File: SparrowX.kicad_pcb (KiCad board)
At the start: 4 copper layers, 31.6 x 26.6 mm, 25 parts, among them J1 NORTH, J2 SOUTH, J3 WEST, J4 EAST, U1 TPS629210-Q1, U2 LD49100PU33RY, U3 STM32G0B1CBU6, U4 TCAN332G, U5 TCAN332G

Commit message: Everybody gets more vias!
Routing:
- net /PA0: track 7.64 -> 10.5 mm
- net VDC: track 37.8 -> 39.1 mm
- net /~{RESET}: track 31.0 -> 29.8 mm
- net /CAN0_TX: track 8.87 -> 9.97 mm
- net /PA10: track 18.7 -> 19.2 mm
- net /PB14: track 20.9 -> 21.4 mm
- net GND: vias 29 -> 85
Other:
- board text added: "2"

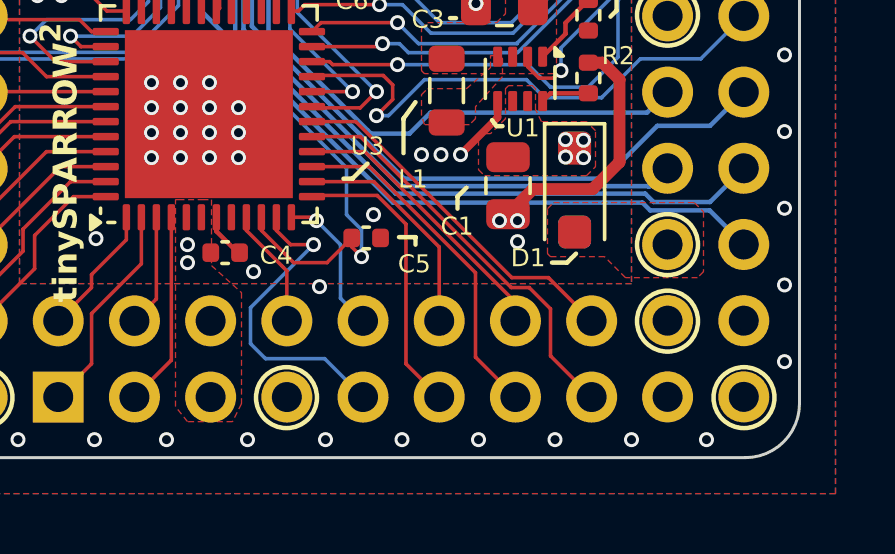
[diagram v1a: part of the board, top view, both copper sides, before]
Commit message: Oops: fix missing PF0 pin
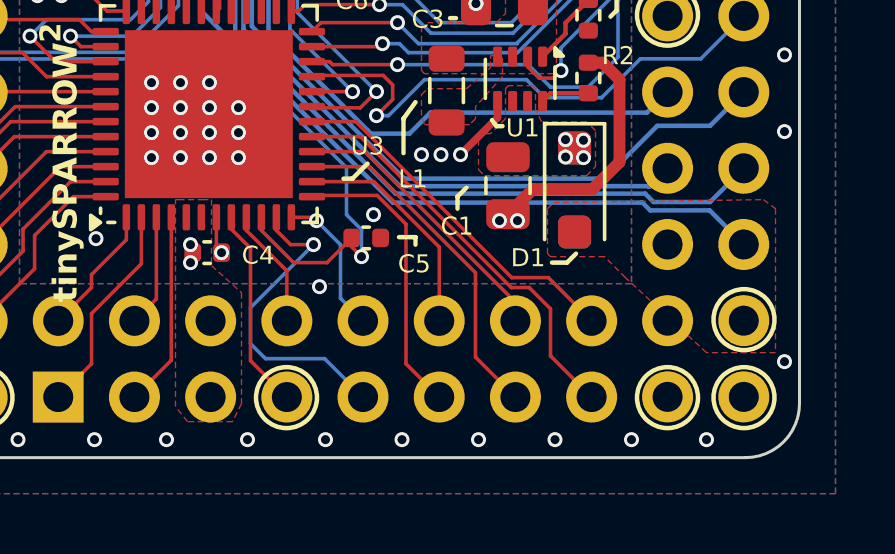
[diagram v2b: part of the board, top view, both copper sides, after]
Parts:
- moved C4 0.60 mm to (166.5, 100.6)
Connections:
- J2 pad 7: GND -> /PF0
- J4 pad 15: VDC -> unconnected-(J4-Pin_15-Pad15)
- J4 pad 17: GND -> unconnected-(J4-Pin_17-Pad17)
- J4 pad 18: unconnected-(J4-Pin_18-Pad18) -> VDC
- J4 pad 19: unconnected-(J4-Pin_19-Pad19) -> GND
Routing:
- net /PF0: track 0.00 -> 6.76 mm
- net VDC: track 39.1 -> 42.0 mm
- net GND: track 12.3 -> 12.0 mm, vias 85 -> 82
- added copper zone on In2.Cu, net VDC
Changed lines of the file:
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@@
 	(net 70 "unconnected-(U5-NC-Pad5)")
 	(net 71 "unconnected-(U5-NC-Pad8)")
-	(net 72 "unconnected-(J4-Pin_19-Pad19)")
-	(net 73 "unconnected-(J4-Pin_18-Pad18)")
+	(net 72 "unconnected-(J4-Pin_17-Pad17)")
+	(net 73 "unconnected-(J4-Pin_15-Pad15)")
 	(net 74 "unconnected-(U2-PG-Pad3)")
 	(footprint "Capacitor_SMD:C_0402_1005Metric"
@@
 	(footprint "Capacitor_SMD:C_0402_1005Metric"
 		(layer "F.Cu")
-		(at 167.0548 100.5672)
+		(at 166.4548 100.5672)
 		(descr "Capacitor SMD 0402 (1005 Metric), square (rectangular) end terminal, IPC_7351 nominal, (Body size source: IPC-SM-782 page 76, https://www.pcb-3d.com/wordpress/wp-content/uploads/ipc-sm-782a_amendment_1_and_2.pdf), generated with kicad-footprint-generator")
 		(tags "capacitor")
@@
 			(layers "*.Cu" "*.Mask")
 			(remove_unused_layers no)
-			(net 1 "GND")
+			(net 52 "/PF0")
 			(pinfunction "Pin_7")
 			(pintype "passive")
@@
 			(layers "*.Cu" "*.Mask")
 			(remove_unused_layers no)
-			(net 10 "VDC")
+			(net 73 "unconnected-(J4-Pin_15-Pad15)")
 			(pinfunction "Pin_15")
-			(pintype "passive")
+			(pintype "passive+no_connect")
 		)
 		(pad "16" thru_hole oval
@@
 			(layers "*.Cu" "*.Mask")
 			(remove_unused_layers no)
-			(net 1 "GND")
+			(net 72 "unconnected-(J4-Pin_17-Pad17)")
 			(pinfunction "Pin_17")
-			(pintype "passive")
+			(pintype "passive+no_connect")
 		)
 		(pad "18" thru_hole oval
@@
 			(layers "*.Cu" "*.Mask")
 			(remove_unused_layers no)
-			(net 73 "unconnected-(J4-Pin_18-Pad18)")
+			(net 10 "VDC")
 			(pinfunction "Pin_18")
-			(pintype "passive+no_connect")
+			(pintype "passive")
 		)
 		(pad "19" thru_hole oval
@@
 			(layers "*.Cu" "*.Mask")
 			(remove_unused_layers no)
-			(net 72 "unconnected-(J4-Pin_19-Pad19)")
+			(net 1 "GND")
 			(pinfunction "Pin_19")
-			(pintype "passive+no_connect")
+			(pintype "passive")
 		)
 		(pad "20" thru_hole oval
@@
 	)
 	(gr_circle
-		(center 181.8 102.85)
-		(end 181.8 101.834)
+		(center 181.8 105.4)
+		(end 181.8 104.384)
 		(stroke
 			(width 0.15)
@@
 	)
 	(gr_circle
-		(center 181.8 100.3)
-		(end 182.816 100.3)
+		(center 184.35 102.8)
+		(end 185.366 102.8)
 		(stroke
 			(width 0.15)
@@
 	)
 	(segment
-		(start 166.762136 99.387764)
-		(end 166.762136 99.853756)
-		(width 0.15)
+		(start 176.1378 96.0622)
+		(end 174.9 97.3)
+		(width 0.25)
 		(layer "F.Cu")
 		(net 1)
 	)
 	(segment
-		(start 167.47558 100.5672)
-		(end 167.5348 100.5672)
-		(width 0.15)
+		(start 177.317599 98.45)
+		(end 176.4828 99.284799)
+		(width 0.4)
 		(layer "F.Cu")
 		(net 1)
 	)
 	(segment
-		(start 176.1378 96.0622)
-		(end 174.9 97.3)
-		(width 0.25)
+		(start 166.762136 99.387764)
+		(end 166.762136 100.394536)
+		(width 0.12)
 		(layer "F.Cu")
 		(net 1)
 	)
 	(segment
-		(start 177.317599 98.45)
-		(end 176.4828 99.284799)
-		(width 0.4)
+		(start 166.762136 100.394536)
+		(end 166.9348 100.5672)
+		(width 0.12)
 		(layer "F.Cu")
 		(net 1)
@@
 		(net 1)
 	)
-	(segment
-		(start 166.762136 99.853756)
-		(end 167.47558 100.5672)
-		(width 0.15)
-		(layer "F.Cu")
-		(net 1)
-	)
 	(via
 		(at 161.6 92)
@@
 	)
 	(via
-		(at 168 101.2)
-		(size 0.5)
-		(drill 0.3)
-		(layers "F.Cu" "B.Cu")
-		(free yes)
-		(net 1)
-	)
-	(via
 		(at 166.533332 95.733333)
 		(size 0.5)
@@
 	)
 	(via
-		(at 176.8 100.2)
-		(size 0.5)
-		(drill 0.3)
-		(layers "F.Cu" "B.Cu")
-		(free yes)
-		(net 1)
-	)
-	(via
 		(at 165.1 106.8)
 		(size 0.5)
@@
 	)
 	(via
-		(at 185.7 101.64375)
-		(size 0.5)
-		(drill 0.3)
-		(layers "F.Cu" "B.Cu")
-		(free yes)
-		(net 1)
-	)
-	(via
 		(at 162.75 100.1)
 		(size 0.5)
@@
 	)
 	(via
-		(at 185.7 99.0875)
-		(size 0.5)
-		(drill 0.3)
-		(layers "F.Cu" "B.Cu")
-		(free yes)
-		(net 1)
-	)
-	(via
 		(at 175.415201 92.262801)
 		(size 0.5)
@@
 	)
 	(via
+		(at 166.9348 100.5672)
+		(size 0.5)
+		(drill 0.3)
+		(layers "F.Cu" "B.Cu")
+		(net 1)
+	)
+	(via
 		(at 178.15 81.2)
 		(size 0.5)
@@
 	)
 	(via
-		(at 165.8 100.9)
+		(at 165.9 100.9)
 		(size 0.5)
 		(drill 0.3)
@@
 	)
 	(via
-		(at 165.8 100.3)
+		(at 165.9 100.3)
 		(size 0.5)
 		(drill 0.3)
@@
 	)
 	(segment
-		(start 162.7844 83.8218)
-		(end 162.7844 86.5844)
+		(start 162.7844 86.5844)
+		(end 163.5 87.3)
 		(width 0.4)
 		(layer "In2.Cu")
@@
 	)
 	(segment
-		(start 162.7844 86.5844)
-		(end 163.5 87.3)
+		(start 169.5 98.3)
+		(end 172.8 98.3)
 		(width 0.4)
 		(layer "In2.Cu")
@@
 	)
 	(segment
-		(start 163.5 94.3)
-		(end 162 95.8)
+		(start 175.2 100.7)
+		(end 179.6 100.7)
 		(width 0.4)
 		(layer "In2.Cu")
@@
 	)
 	(segment
-		(start 163 99.1)
-		(end 168.7 99.1)
+		(start 179.6 100.7)
+		(end 180.4448 101.5448)
 		(width 0.4)
 		(layer "In2.Cu")
@@
 	)
 	(segment
-		(start 162 98.1)
-		(end 163 99.1)
+		(start 163.5 94.3)
+		(end 162 95.8)
 		(width 0.4)
 		(layer "In2.Cu")
@@
 	)
 	(segment
-		(start 169.5 98.3)
-		(end 172.8 98.3)
+		(start 172.8 98.3)
+		(end 175.2 100.7)
 		(width 0.4)
 		(layer "In2.Cu")
@@
 	)
 	(segment
-		(start 179.1 101.1)
-		(end 179.9052 100.2948)
+		(start 163 99.1)
+		(end 168.7 99.1)
 		(width 0.4)
 		(layer "In2.Cu")
@@
 	)
 	(segment
-		(start 179.9052 100.2948)
-		(end 181.8024 100.2948)
+		(start 162 95.8)
+		(end 162 98.1)
 		(width 0.4)
 		(layer "In2.Cu")
@@
 	)
 	(segment
-		(start 163.5 87.3)
-		(end 163.5 94.3)
+		(start 180.4448 101.5448)
+		(end 183.0524 101.5448)
 		(width 0.4)
 		(layer "In2.Cu")
@@
 	)
 	(segment
-		(start 175.6 101.1)
-		(end 179.1 101.1)
+		(start 162 98.1)
+		(end 163 99.1)
 		(width 0.4)
 		(layer "In2.Cu")
@@
 	)
 	(segment
-		(start 162 95.8)
-		(end 162 98.1)
+		(start 161.4944 82.5318)
+		(end 162.7844 83.8218)
 		(width 0.4)
 		(layer "In2.Cu")
@@
 	)
 	(segment
-		(start 161.4944 82.5318)
-		(end 162.7844 83.8218)
+		(start 163.5 87.3)
+		(end 163.5 94.3)
 		(width 0.4)
 		(layer "In2.Cu")
@@
 	)
 	(segment
-		(start 172.8 98.3)
-		(end 175.6 101.1)
+		(start 183.0524 101.5448)
+		(end 184.3424 102.8348)
+		(width 0.4)
+		(layer "In2.Cu")
+		(net 10)
+	)
+	(segment
+		(start 162.7844 83.8218)
+		(end 162.7844 86.5844)
 		(width 0.4)
 		(layer "In2.Cu")
@@
 	)
 	(segment
+		(start 167.9 100.420944)
+		(end 167.9 104.1692)
+		(width 0.12)
+		(layer "F.Cu")
+		(net 52)
+	)
+	(segment
+		(start 167.262136 99.78308)
+		(end 167.9 100.420944)
+		(width 0.12)
+		(layer "F.Cu")
+		(net 52)
+	)
+	(segment
+		(start 167.9 104.1692)
+		(end 169.1116 105.3808)
+		(width 0.12)
+		(layer "F.Cu")
+		(net 52)
+	)
+	(segment
+		(start 167.262136 99.387764)
+		(end 167.262136 99.78308)
+		(width 0.12)
+		(layer "F.Cu")
+		(net 52)
+	)
+	(segment
 		(start 169.1116 102.8408)
 		(end 169.1116 101.174728)
@@
 		(net 10)
 		(net_name "VDC")
-		(layer "F.Cu")
+		(layers "F.Cu" "In2.Cu")
 		(name "VDC_IN")
 		(hatch edge 0.5)
 		(priority 7)
 		(connect_pads yes
-			(clearance 0.5)
+			(clearance 0.3)
 		)
-		(min_thickness 0.25)
+		(min_thickness 0.15)
 		(filled_areas_thickness no)
 		(fill yes
@@
 		(polygon
 			(pts
-				(xy 177.8 100.6) (xy 177.8 99.1) (xy 178 98.9) (xy 182.7 98.9) (xy 183 99.2) (xy 183 101.2) (xy 182.8 101.4)
+				(xy 177.8 100.6) (xy 177.8 99.1) (xy 178 98.9) (xy 185 98.8) (xy 185.4 99.1) (xy 185.4 103.9) (xy 183.1 103.9)
 				(xy 180.4 101.4) (xy 179.7 100.7) (xy 177.9 100.7)
 			)

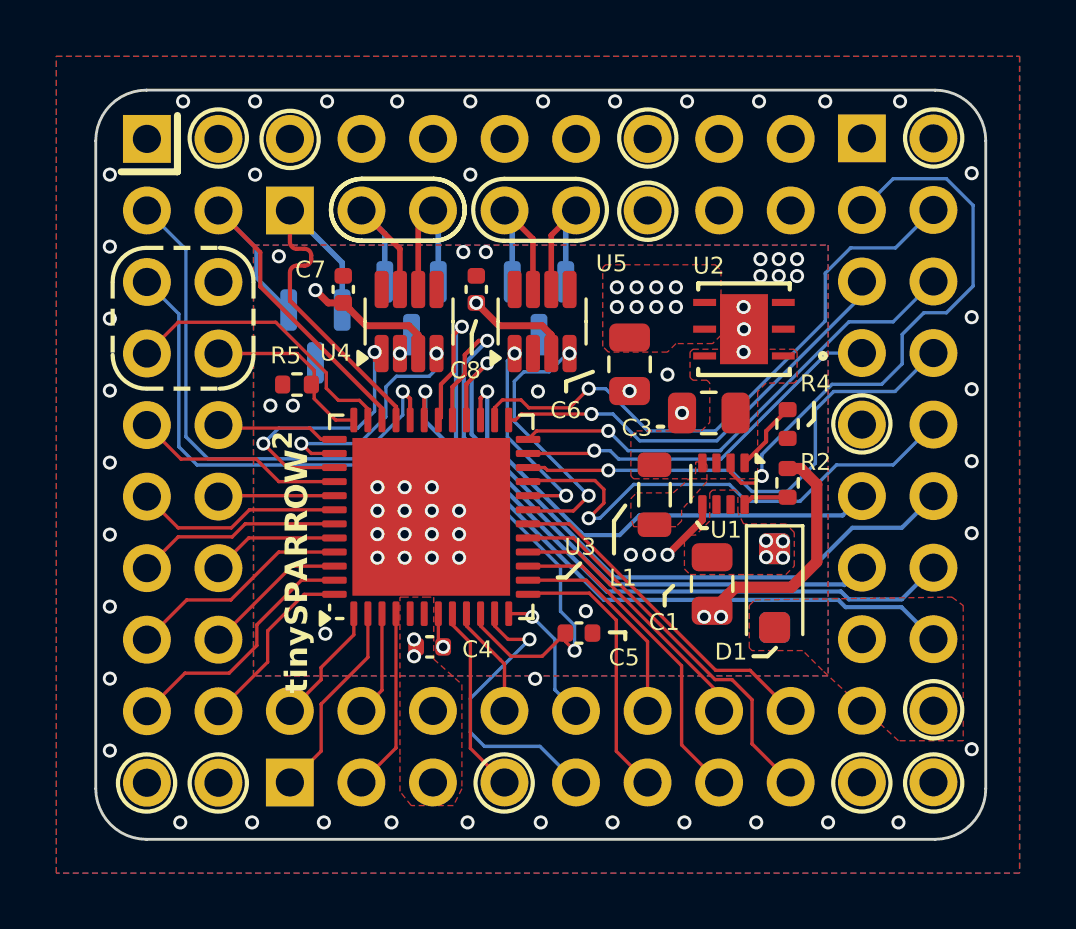
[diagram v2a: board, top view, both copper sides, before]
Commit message: Move power good signal pin for better layout
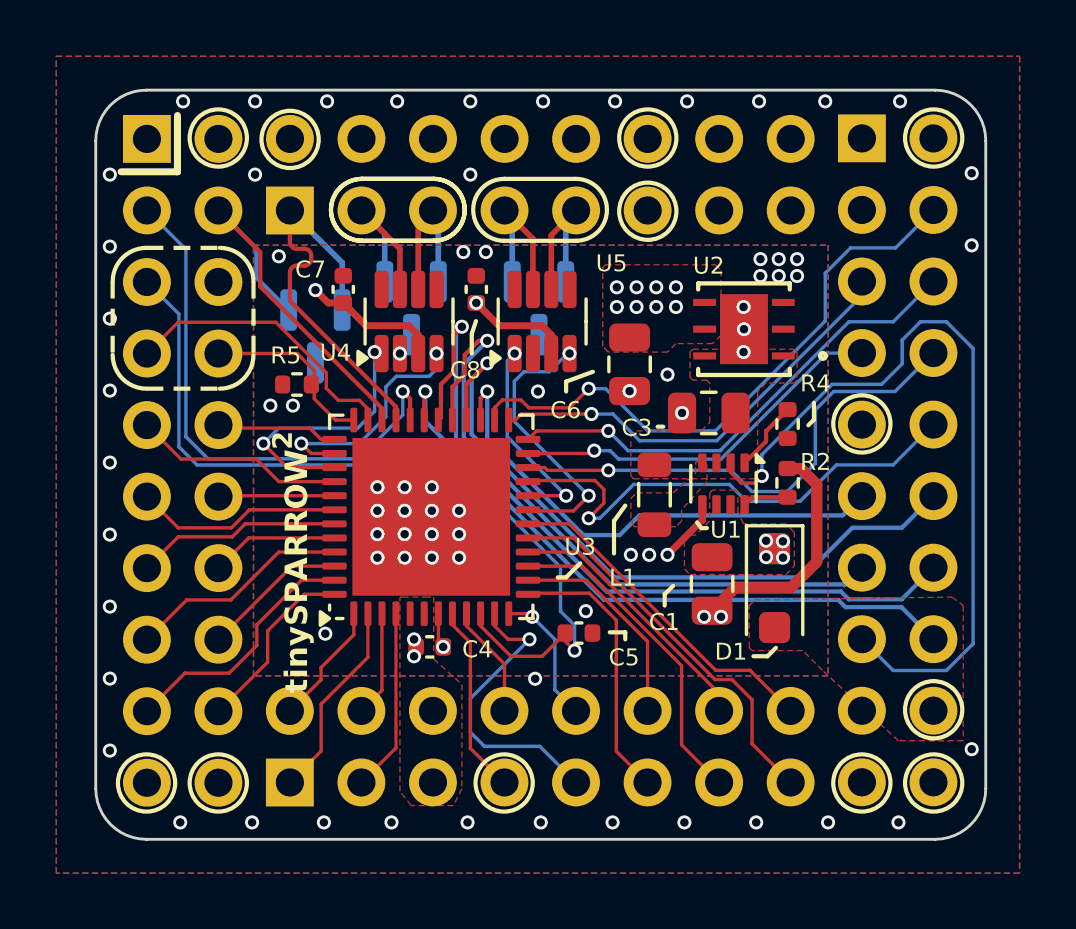
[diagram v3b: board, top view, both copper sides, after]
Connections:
- J4 pad 15: unconnected-(J4-Pin_15-Pad15) -> /P_{GOOD}
- J4 pad 3: /P_{GOOD} -> unconnected-(J4-Pin_3-Pad3)
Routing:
- net /P_{GOOD}: track 20.7 -> 28.1 mm
- net GND: vias 82 -> 79
- added copper zone on In1.Cu, net GND
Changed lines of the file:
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@@
 	(net 71 "unconnected-(U5-NC-Pad8)")
 	(net 72 "unconnected-(J4-Pin_17-Pad17)")
-	(net 73 "unconnected-(J4-Pin_15-Pad15)")
+	(net 73 "unconnected-(J4-Pin_3-Pad3)")
 	(net 74 "unconnected-(U2-PG-Pad3)")
 	(footprint "Capacitor_SMD:C_0402_1005Metric"
@@
 			(layers "*.Cu" "*.Mask")
 			(remove_unused_layers no)
-			(net 57 "/P_{GOOD}")
+			(net 73 "unconnected-(J4-Pin_3-Pad3)")
 			(pinfunction "Pin_3")
-			(pintype "passive")
+			(pintype "passive+no_connect")
 		)
 		(pad "4" thru_hole oval
@@
 			(layers "*.Cu" "*.Mask")
 			(remove_unused_layers no)
-			(net 73 "unconnected-(J4-Pin_15-Pad15)")
+			(net 57 "/P_{GOOD}")
 			(pinfunction "Pin_15")
-			(pintype "passive+no_connect")
+			(pintype "passive")
 		)
 		(pad "16" thru_hole oval
@@
 	)
 	(via
-		(at 185.7 93.975)
-		(size 0.5)
-		(drill 0.3)
-		(layers "F.Cu" "B.Cu")
-		(free yes)
-		(net 1)
-	)
-	(via
 		(at 178.2 86.8)
 		(size 0.5)
@@
 	)
 	(via
-		(at 185.7 91.41875)
-		(size 0.5)
-		(drill 0.3)
-		(layers "F.Cu" "B.Cu")
-		(free yes)
-		(net 1)
-	)
-	(via
 		(at 166.533332 96.566666)
 		(size 0.5)
@@
 	)
 	(via
-		(at 185.7 88.8625)
+		(at 185.7 86.3125)
 		(size 0.5)
 		(drill 0.3)
@@
 	)
 	(via
-		(at 185.7 96.53125)
-		(size 0.5)
-		(drill 0.3)
-		(layers "F.Cu" "B.Cu")
-		(free yes)
-		(net 1)
-	)
-	(via
 		(at 160.25625 83.8)
 		(size 0.5)
@@
 	)
 	(segment
-		(start 182.9124 83.9448)
-		(end 181.8024 85.0548)
+		(start 184.802178 101.4048)
+		(end 182.9124 101.4048)
 		(width 0.12)
 		(layer "B.Cu")
@@
 	)
 	(segment
-		(start 185.75 84.892622)
-		(end 184.802178 83.9448)
+		(start 182.5052 91.2448)
+		(end 183.2324 90.5176)
 		(width 0.12)
 		(layer "B.Cu")
@@
 	)
 	(segment
-		(start 180.744073 91.2448)
-		(end 182.5052 91.2448)
+		(start 183.2324 89.675022)
+		(end 183.882622 89.0248)
 		(width 0.12)
 		(layer "B.Cu")
@@
 	)
 	(segment
-		(start 183.2324 90.5176)
-		(end 183.2324 89.4724)
+		(start 178.25 94.5)
+		(end 178.25 93.738873)
 		(width 0.12)
 		(layer "B.Cu")
@@
 	)
 	(segment
-		(start 182.5052 91.2448)
-		(end 183.2324 90.5176)
+		(start 185.75 89.972622)
+		(end 185.75 100.456978)
 		(width 0.12)
 		(layer "B.Cu")
@@
 	)
 	(segment
-		(start 183.2324 89.4724)
-		(end 184 88.7048)
+		(start 184.802178 89.0248)
+		(end 185.75 89.972622)
 		(width 0.12)
 		(layer "B.Cu")
@@
 	)
 	(segment
-		(start 185.75 87.756978)
-		(end 185.75 84.892622)
+		(start 180.744073 91.2448)
+		(end 182.5052 91.2448)
 		(width 0.12)
 		(layer "B.Cu")
@@
 	)
 	(segment
-		(start 178.25 94.5)
-		(end 178.25 93.738873)
+		(start 183.882622 89.0248)
+		(end 184.802178 89.0248)
 		(width 0.12)
 		(layer "B.Cu")
@@
 	)
 	(segment
-		(start 184.802178 88.7048)
-		(end 185.75 87.756978)
+		(start 185.75 100.456978)
+		(end 184.802178 101.4048)
 		(width 0.12)
 		(layer "B.Cu")
@@
 	)
 	(segment
-		(start 184 88.7048)
-		(end 184.802178 88.7048)
+		(start 183.2324 90.5176)
+		(end 183.2324 89.675022)
 		(width 0.12)
 		(layer "B.Cu")
@@
 	)
 	(segment
-		(start 184.802178 83.9448)
-		(end 182.9124 83.9448)
+		(start 182.9124 101.4048)
+		(end 181.8024 100.2948)
 		(width 0.12)
 		(layer "B.Cu")
@@
 			)
 		)
+	)
+	(zone
+		(net 1)
+		(net_name "GND")
+		(layer "In1.Cu")
+		(name "GND_HELPER_IN1")
+		(hatch edge 0.5)
+		(priority 8)
+		(connect_pads
+			(clearance 0.3)
+		)
+		(min_thickness 0.15)
+		(filled_areas_thickness no)
+		(fill yes
+			(thermal_gap 0.3)
+			(thermal_bridge_width 0.4)
+		)
+		(polygon
+			(pts
+				(xy 173 110) (xy 173 91.5) (xy 191 91.5) (xy 191 110)
+			)
+		)
